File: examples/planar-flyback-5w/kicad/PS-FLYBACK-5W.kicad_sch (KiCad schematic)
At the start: 29 parts, among them J1 18-36 V DC, J2 5 V / 1 A isolated, T1 PLANAR 4:2 / Lm 13.12uH, U1 LT8302IS8E#PBF

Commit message: Upgrade flyback snubber to 2 W 2512 and regenerate A5 handoff
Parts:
- R6: value 39R 0.75 W -> 39R 2 W; footprint Flyback:R_1206_3216Metric -> Flyback:R_EverOhms_CRH2512; LCSC C6683830 -> C175263; MPN SR1206FR-7T39RL -> CRH2512F39R0E04Z; Manufacturer Yageo -> Ever Ohms Tech
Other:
- note added: "18-36 V input | isolated 5 V / 1 A | A5 engineering prototype"
- note removed: "18-36 V input | isolated 5 V / 1 A | A4 engineering prototype"
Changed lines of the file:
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@@
 (kicad_sch (version 20250114) (generator "eeschema") (paper "A4")
-(title_block (title "18-36 V to isolated 5 V / 1 A planar flyback") (date "2026-10-08") (rev "A4-development") (company "Planar Studio example"))
+(title_block (title "18-36 V to isolated 5 V / 1 A planar flyback") (date "2026-10-09") (rev "A5-development") (company "Planar Studio example"))

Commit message: fix(flyback): center secondary routing and strengthen preload margin
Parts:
- R7: value 220R 0.25 W -> 180R 0.25 W; LCSC C137353 -> C137380; MPN RC1206FR-07220RL -> RC1206FR-07180RL
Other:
- note added: "18-36 V input | isolated 5 V / 1 A | A6 engineering prototype"
- note removed: "18-36 V input | isolated 5 V / 1 A | A5 engineering prototype"
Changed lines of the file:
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@@
 (kicad_sch (version 20250114) (generator "eeschema") (paper "A4")
-(title_block (title "18-36 V to isolated 5 V / 1 A planar flyback") (date "2026-10-09") (rev "A5-development") (company "Planar Studio example"))
+(title_block (title "18-36 V to isolated 5 V / 1 A planar flyback") (date "2026-10-16") (rev "A6-development") (company "Planar Studio example"))

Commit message: fix(flyback): select OSP and replace short-stock UVLO resistor
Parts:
- R1: LCSC C245991 -> C25821; MPN RC0603FR-07649KL -> 0603WAF6493T5E; Manufacturer Yageo -> UNI-ROYAL
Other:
- note added: "18-36 V input | isolated 5 V / 1 A | A7 engineering prototype"
- note removed: "18-36 V input | isolated 5 V / 1 A | A6 engineering prototype"
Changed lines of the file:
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@@
 (kicad_sch (version 20250114) (generator "eeschema") (paper "A4")
-(title_block (title "18-36 V to isolated 5 V / 1 A planar flyback") (date "2026-10-16") (rev "A6-development") (company "Planar Studio example"))
+(title_block (title "18-36 V to isolated 5 V / 1 A planar flyback") (date "2026-10-16") (rev "A7-development") (company "Planar Studio example"))

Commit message: Fix flyback SW winding short and publish verified A8 files
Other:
- note added: "18-36 V input | isolated 5 V / 1 A | A8 engineering prototype"
- note removed: "18-36 V input | isolated 5 V / 1 A | A7 engineering prototype"
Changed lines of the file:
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@@
 (kicad_sch (version 20250114) (generator "eeschema") (paper "A4")
-(title_block (title "18-36 V to isolated 5 V / 1 A planar flyback") (date "2026-10-16") (rev "A7-development") (company "Planar Studio example"))
+(title_block (title "18-36 V to isolated 5 V / 1 A planar flyback") (date "2026-10-19") (rev "A8-development") (company "Planar Studio example"))

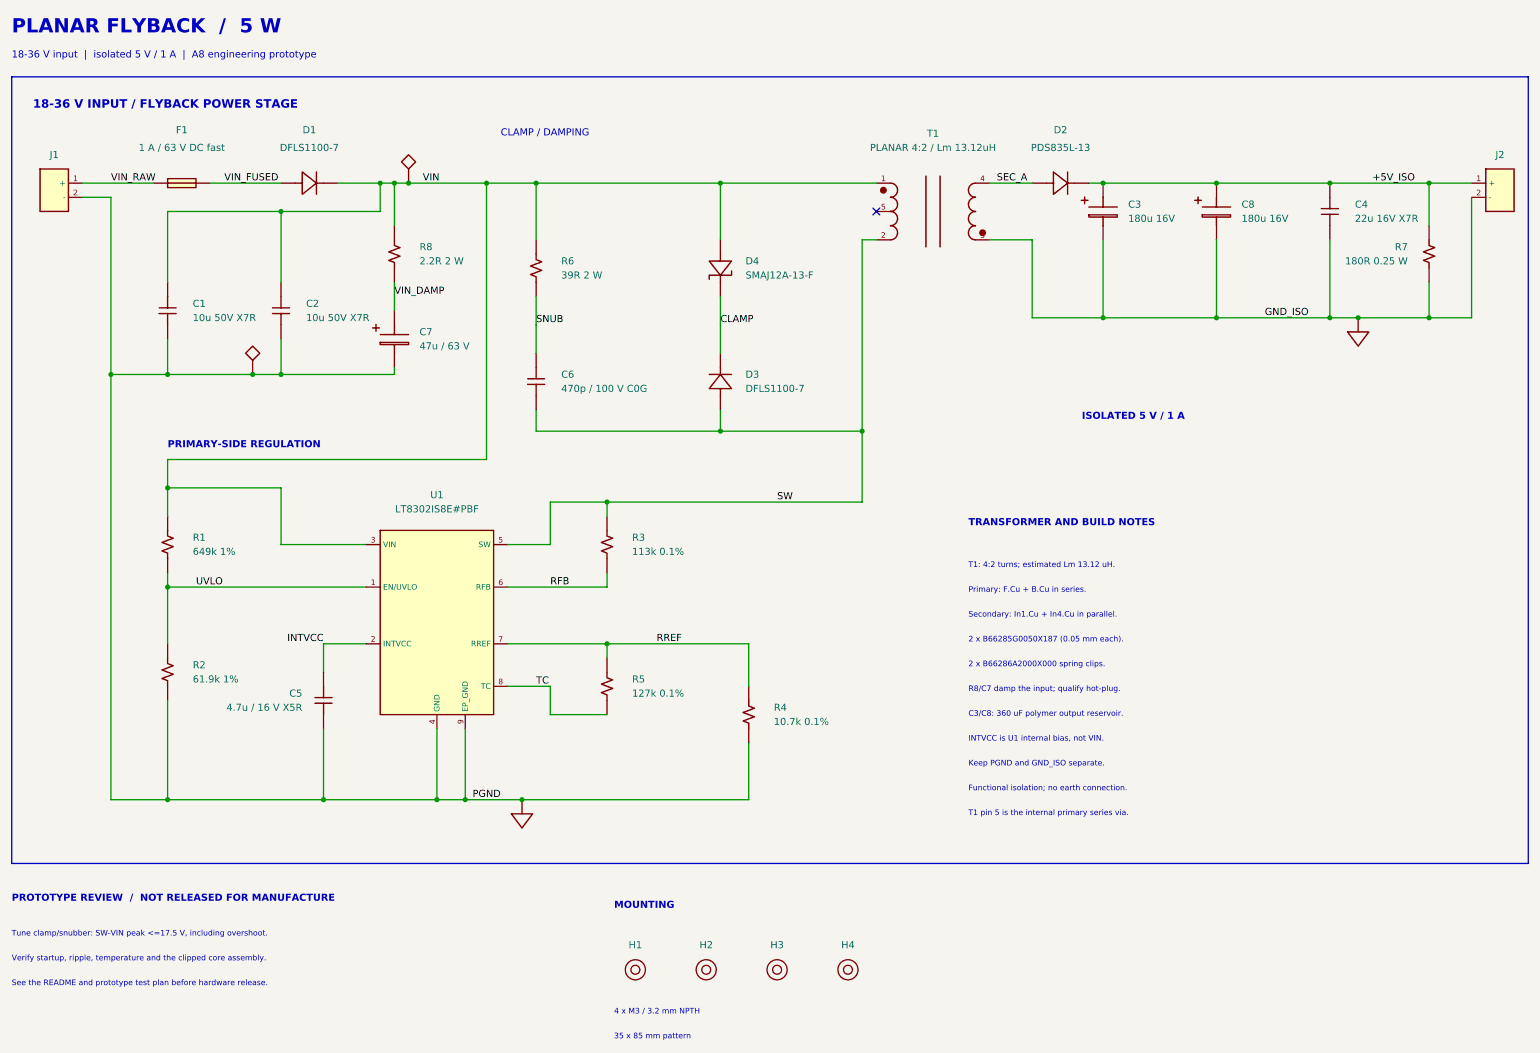
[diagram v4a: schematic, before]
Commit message: Fix flyback turn spacing and document PCB integration pitfalls
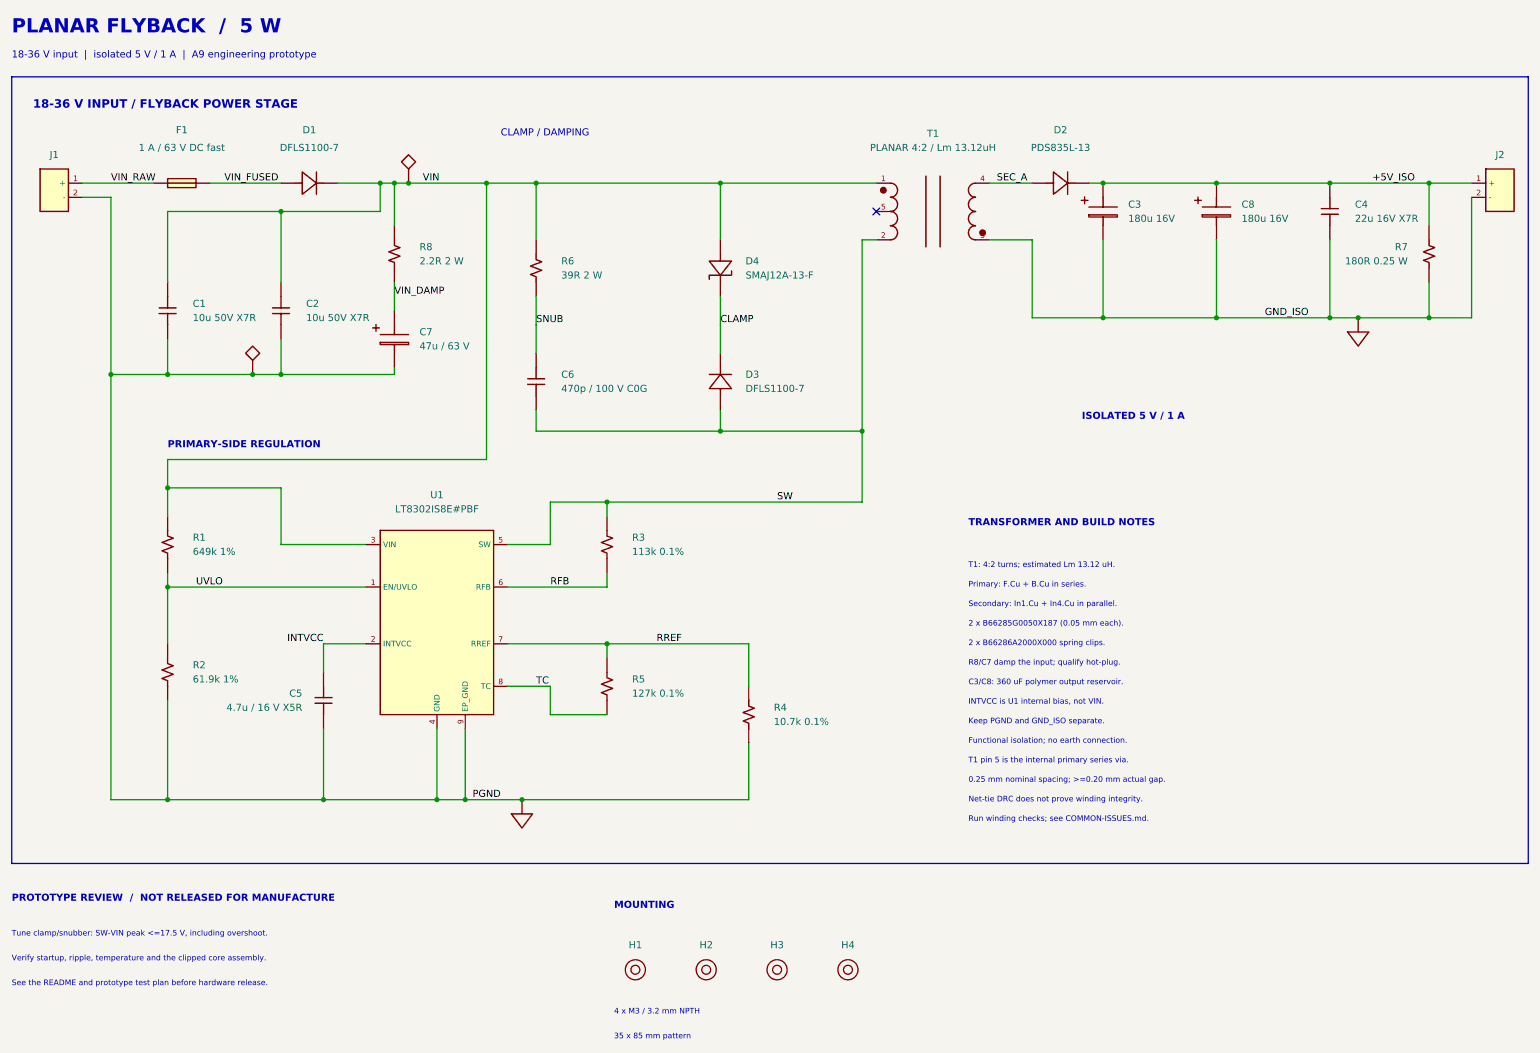
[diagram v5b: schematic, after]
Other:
- note added: "0.25 mm nominal spacing; >=0.20 mm actual gap."
- note added: "18-36 V input | isolated 5 V / 1 A | A9 engineering prototype"
- note added: "Net-tie DRC does not prove winding integrity."
- note added: "Run winding checks; see COMMON-ISSUES.md."
- note removed: "18-36 V input | isolated 5 V / 1 A | A8 engineering prototype"
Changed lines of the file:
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@@
 (kicad_sch (version 20250114) (generator "eeschema") (paper "A4")
-(title_block (title "18-36 V to isolated 5 V / 1 A planar flyback") (date "2026-10-19") (rev "A8-development") (company "Planar Studio example"))
+(title_block (title "18-36 V to isolated 5 V / 1 A planar flyback") (date "2026-10-19") (rev "A9-development") (company "Planar Studio example"))

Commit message: Fix flyback winding and via clearances in A10
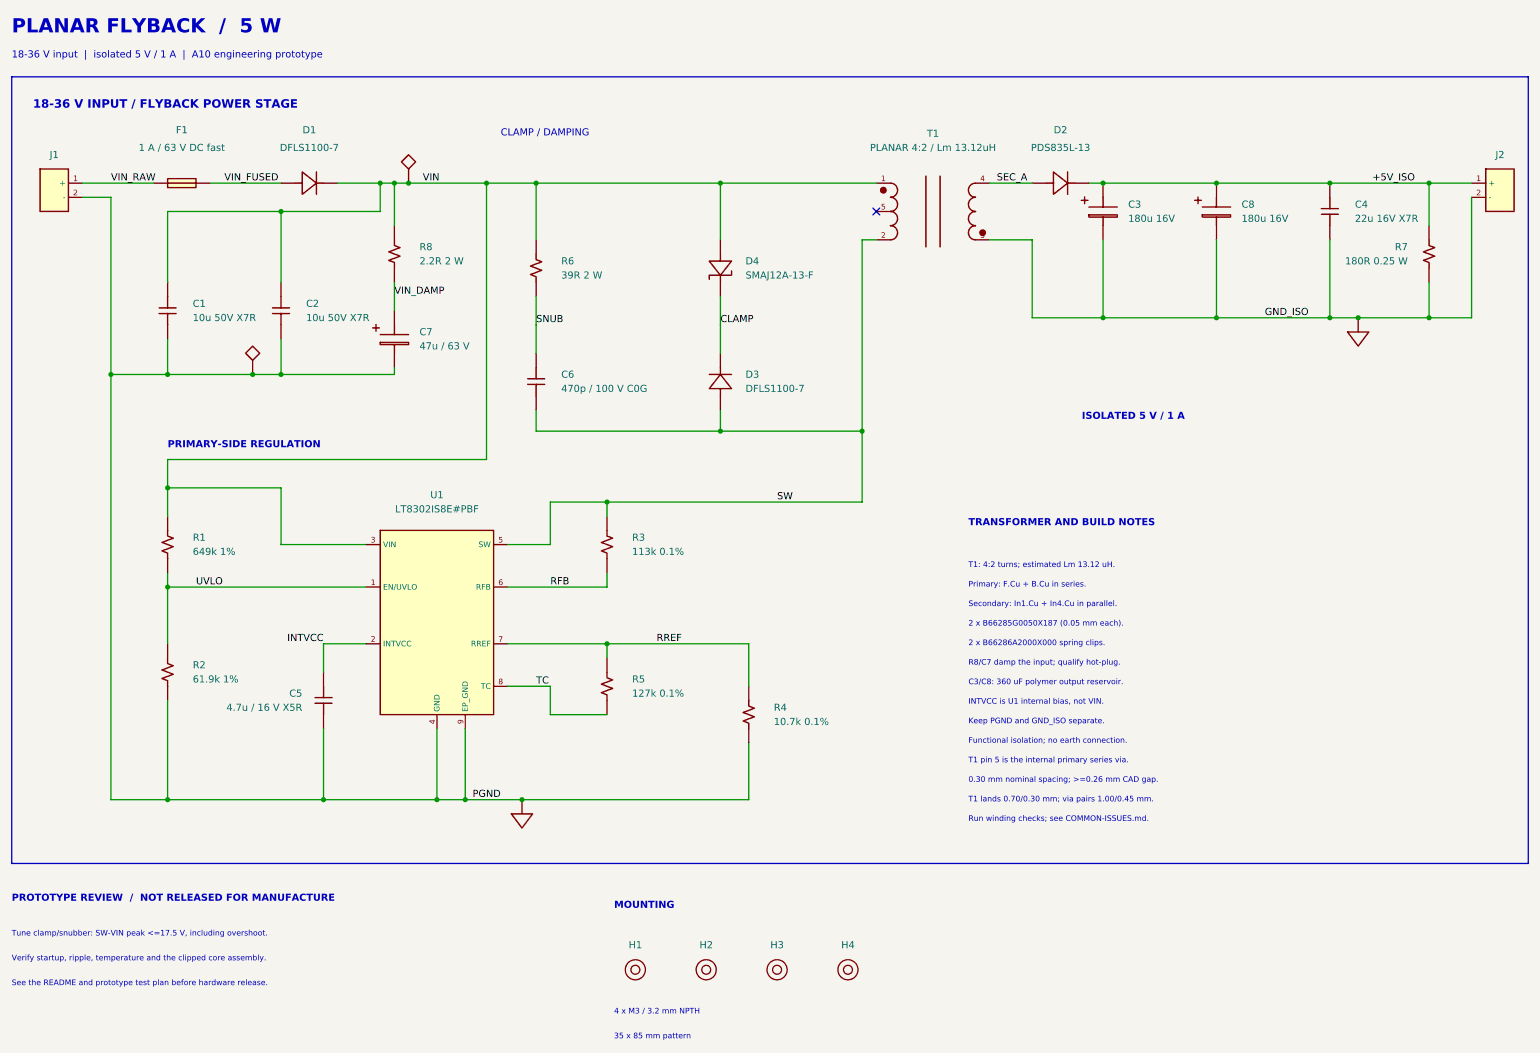
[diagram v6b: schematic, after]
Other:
- note added: "0.30 mm nominal spacing; >=0.26 mm CAD gap."
- note added: "18-36 V input | isolated 5 V / 1 A | A10 engineering prototype"
- note added: "T1 lands 0.70/0.30 mm; via pairs 1.00/0.45 mm."
- note removed: "0.25 mm nominal spacing; >=0.20 mm actual gap."
- note removed: "18-36 V input | isolated 5 V / 1 A | A9 engineering prototype"
- note removed: "Net-tie DRC does not prove winding integrity."
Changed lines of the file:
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@@
 (kicad_sch (version 20250114) (generator "eeschema") (paper "A4")
-(title_block (title "18-36 V to isolated 5 V / 1 A planar flyback") (date "2026-10-19") (rev "A9-development") (company "Planar Studio example"))
+(title_block (title "18-36 V to isolated 5 V / 1 A planar flyback") (date "2026-10-19") (rev "A10-development") (company "Planar Studio example"))
